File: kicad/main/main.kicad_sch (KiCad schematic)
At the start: 29 parts, among them J1 Barrel_Jack_MountingPin, SW1 Reset, SW2 SW_DIP_x08, U1 GAL16V8, U2 Z80CPU, U3 DS1813-5+, U4 AS6C4008-55PCN, U5 L7805, U6 74HC273, U7 27C512, U8 74HC244, X1 4 MHz

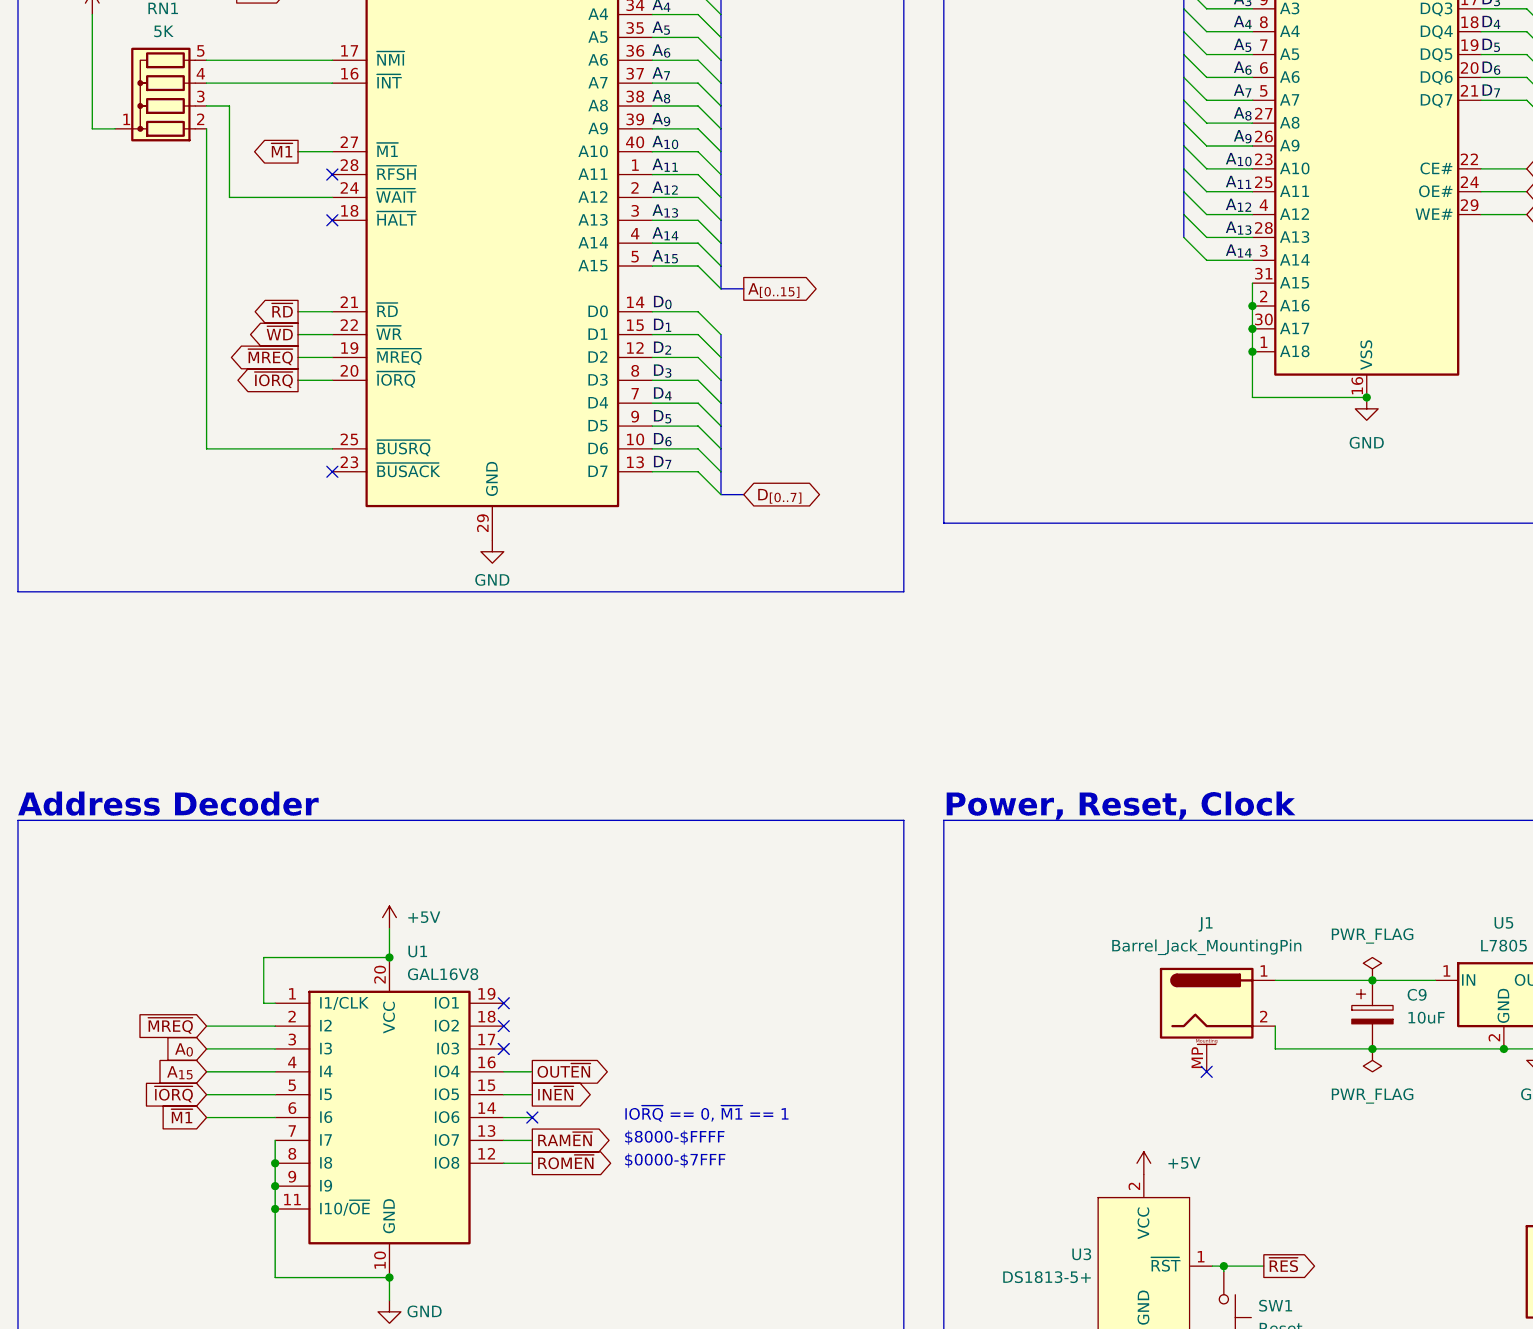
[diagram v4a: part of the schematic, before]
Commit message: Fix RAM CE2, add /RFSH
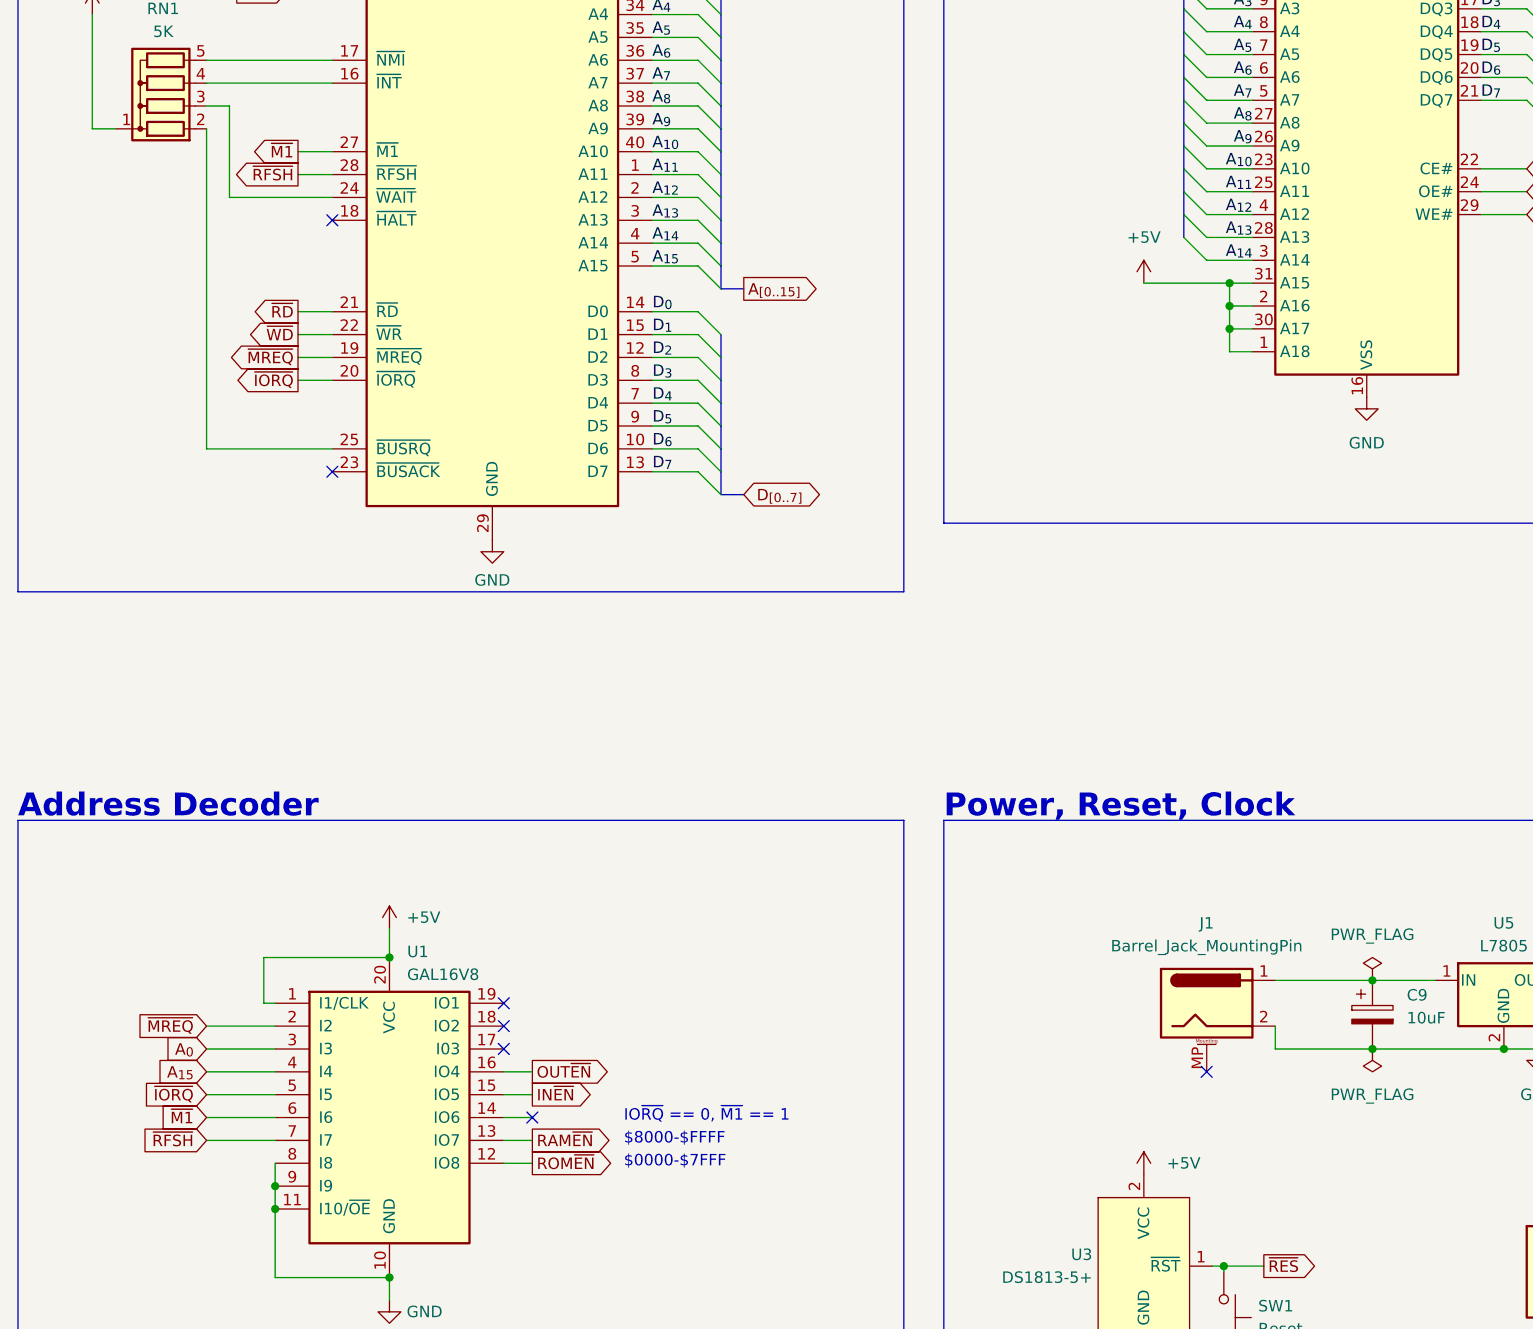
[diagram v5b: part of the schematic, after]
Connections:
- net +5V: now also U4.1 (A18), U4.2 (A16), U4.30 (A17), U4.31 (A15)
- net GND: no longer U1.7 (I7), U4.1 (A18), U4.2 (A16), U4.30 (A17), U4.31 (A15)
- net ~{RFSH}: now reaches U2.28 (~{RFSH})
- net ~{RFSH}: now also U1.7 (I7)
- no-connect marks 12 -> 11
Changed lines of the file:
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@@
   (junction (at 302.26 166.37) (diameter 0) (color 0 0 0 0)
   )
+  (junction (at 151.13 74.295) (diameter 0) (color 0 0 0 0)
+  )
   (junction (at 68.58 219.075) (diameter 0) (color 0 0 0 0)
   )
@@
   (junction (at 302.26 171.45) (diameter 0) (color 0 0 0 0)
   )
-  (junction (at 153.67 76.835) (diameter 0) (color 0 0 0 0)
-  )
   (junction (at 167.005 149.225) (diameter 0) (color 0 0 0 0)
   )
@@
   (junction (at 302.26 168.91) (diameter 0) (color 0 0 0 0)
   )
-  (junction (at 153.67 79.375) (diameter 0) (color 0 0 0 0)
-  )
   (junction (at 333.375 173.99) (diameter 0) (color 0 0 0 0)
   )
@@
   (junction (at 83.82 231.775) (diameter 0) (color 0 0 0 0)
   )
-  (junction (at 166.37 84.455) (diameter 0) (color 0 0 0 0)
-  )
   (junction (at 83.82 219.075) (diameter 0) (color 0 0 0 0)
   )
@@
   (junction (at 335.915 176.53) (diameter 0) (color 0 0 0 0)
   )
+  (junction (at 151.13 76.835) (diameter 0) (color 0 0 0 0)
+  )
   (junction (at 337.82 181.61) (diameter 0) (color 0 0 0 0)
   )
   (junction (at 60.96 219.075) (diameter 0) (color 0 0 0 0)
   )
+  (junction (at 151.13 71.755) (diameter 0) (color 0 0 0 0)
+  )
   (junction (at 53.34 231.775) (diameter 0) (color 0 0 0 0)
   )
   (junction (at 45.72 231.775) (diameter 0) (color 0 0 0 0)
   )
-  (junction (at 153.67 74.295) (diameter 0) (color 0 0 0 0)
-  )
   (junction (at 64.77 231.775) (diameter 0) (color 0 0 0 0)
   )
@@
   )
   (junction (at 45.085 172.085) (diameter 0) (color 0 0 0 0)
-  )
-  (junction (at 45.085 169.545) (diameter 0) (color 0 0 0 0)
   )
   (no_connect (at 73.66 164.465))
@@
   (no_connect (at 70.485 156.845))
   (no_connect (at 70.485 151.765))
-  (no_connect (at 51.435 59.69))
   (bus_entry (at 92.075 87.63) (size 2.54 2.54)
     (stroke (width 0) (type default))
@@
     (stroke (width 0) (type default))
   )
-  (wire (pts (xy 153.67 79.375) (xy 153.67 84.455))
-    (stroke (width 0) (type default))
-  )
   (wire (pts (xy 247.015 54.61) (xy 241.935 54.61))
     (stroke (width 0) (type default))
@@
     (stroke (width 0) (type default))
   )
-  (wire (pts (xy 45.085 167.005) (xy 45.085 169.545))
-    (stroke (width 0) (type default))
-  )
   (bus (pts (xy 186.69 36.195) (xy 186.69 38.735))
     (stroke (width 0) (type default))
@@
     (stroke (width 0) (type default))
   )
+  (wire (pts (xy 151.13 74.295) (xy 153.67 74.295))
+    (stroke (width 0) (type default))
+  )
   (wire (pts (xy 320.675 153.67) (xy 320.675 161.29))
     (stroke (width 0) (type default))
@@
     (stroke (width 0) (type default))
   )
+  (wire (pts (xy 151.13 79.375) (xy 153.67 79.375))
+    (stroke (width 0) (type default))
+  )
   (bus (pts (xy 239.395 52.07) (xy 239.395 49.53))
     (stroke (width 0) (type default))
@@
     (stroke (width 0) (type default))
   )
-  (wire (pts (xy 153.67 71.755) (xy 153.67 74.295))
-    (stroke (width 0) (type default))
-  )
   (bus (pts (xy 146.05 31.115) (xy 139.7 31.115))
     (stroke (width 0) (type default))
@@
     (stroke (width 0) (type default))
   )
+  (wire (pts (xy 151.13 76.835) (xy 151.13 74.295))
+    (stroke (width 0) (type default))
+  )
   (bus (pts (xy 239.395 62.23) (xy 239.395 59.69))
     (stroke (width 0) (type default))
@@
     (stroke (width 0) (type default))
   )
+  (wire (pts (xy 151.13 74.295) (xy 151.13 71.755))
+    (stroke (width 0) (type default))
+  )
   (wire (pts (xy 363.22 176.53) (xy 368.3 176.53))
     (stroke (width 0) (type default))
@@
     (stroke (width 0) (type default))
   )
+  (wire (pts (xy 141.605 71.755) (xy 151.13 71.755))
+    (stroke (width 0) (type default))
+  )
   (wire (pts (xy 267.335 36.83) (xy 272.415 36.83))
     (stroke (width 0) (type default))
@@
     (stroke (width 0) (type default))
   )
-  (wire (pts (xy 153.67 84.455) (xy 166.37 84.455))
+  (wire (pts (xy 151.13 76.835) (xy 153.67 76.835))
     (stroke (width 0) (type default))
   )
@@
     (stroke (width 0) (type default))
   )
+  (wire (pts (xy 151.13 71.755) (xy 153.67 71.755))
+    (stroke (width 0) (type default))
+  )
   (wire (pts (xy 86.995 44.45) (xy 92.075 44.45))
     (stroke (width 0) (type default))
@@
     (stroke (width 0) (type default))
   )
+  (wire (pts (xy 51.435 59.69) (xy 47.625 59.69))
+    (stroke (width 0) (type default))
+  )
   (wire (pts (xy 232.41 179.705) (xy 237.49 179.705))
     (stroke (width 0) (type default))
@@
     (stroke (width 0) (type default))
   )
+  (wire (pts (xy 37.465 167.005) (xy 45.085 167.005))
+    (stroke (width 0) (type default))
+  )
   (bus (pts (xy 146.05 59.055) (xy 146.05 56.515))
     (stroke (width 0) (type default))
@@
     (stroke (width 0) (type default))
   )
-  (wire (pts (xy 153.67 76.835) (xy 153.67 79.375))
-    (stroke (width 0) (type default))
-  )
   (wire (pts (xy 150.495 180.975) (xy 149.225 180.975))
     (stroke (width 0) (type default))
   )
-  (wire (pts (xy 153.67 74.295) (xy 153.67 76.835))
-    (stroke (width 0) (type default))
-  )
   (bus (pts (xy 274.955 41.91) (xy 274.955 44.45))
     (stroke (width 0) (type default))
@@
   )
   (wire (pts (xy 247.015 64.77) (xy 241.935 64.77))
+    (stroke (width 0) (type default))
+  )
+  (wire (pts (xy 151.13 79.375) (xy 151.13 76.835))
     (stroke (width 0) (type default))
   )
@@
     )
   )
+  (global_label "~{RFSH}" (shape input) (at 37.465 167.005 180) (fields_autoplaced)
+    (effects (font (size 1.27 1.27)) (justify right))
+    (property "Intersheetrefs" "${INTERSHEET_REFS}" (at 29.6606 167.005 0)
+      (effects (font (size 1.27 1.27)) (justify right) hide)
+    )
+  )
   (global_label "CLK" (shape output) (at 196.85 181.61 0) (fields_autoplaced)
     (effects (font (size 1.27 1.27)) (justify left))
@@
     (property "Intersheetrefs" "${INTERSHEET_REFS}" (at 193.3453 59.055 0)
       (effects (font (size 1.27 1.27)) (justify left) hide)
+    )
+  )
+  (global_label "~{RFSH}" (shape output) (at 47.625 59.69 180) (fields_autoplaced)
+    (effects (font (size 1.27 1.27)) (justify right))
+    (property "Intersheetrefs" "${INTERSHEET_REFS}" (at 39.8206 59.69 0)
+      (effects (font (size 1.27 1.27)) (justify right) hide)
     )
   )
@@
         )
       )
+    )
+  )
+  (symbol (lib_id "power:+5V") (at 141.605 71.755 0) (unit 1)
+    (in_bom yes) (on_board yes) (dnp no) (fields_autoplaced)
+    (property "Reference" "#PWR025" (at 141.605 75.565 0)
+      (effects (font (size 1.27 1.27)) hide)
+    )
+    (property "Value" "+5V" (at 141.605 66.675 0)
+      (effects (font (size 1.27 1.27)))
+    )
+    (property "Footprint" "" (at 141.605 71.755 0)
+      (effects (font (size 1.27 1.27)) hide)
+    )
+    (property "Datasheet" "" (at 141.605 71.755 0)
+      (effects (font (size 1.27 1.27)) hide)
+    )
+    (pin "1")
+    (instances
+      (project "main"
+        (path "/234daa3c-bbc3-4e0e-9846-fc4a6309b941"
+          (reference "#PWR025") (unit 1)
+        )
+      )

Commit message: Add new buffers
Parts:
- added U10, U11, U12: 74LS244, Package_DIP:DIP-20_W7.62mm_Socket, symbol 74xx:74LS244
- added U13: 74LS14, symbol 74xx:74LS14
- added U9: 74LS245, Package_DIP:DIP-20_W7.62mm_Socket, symbol 74xx:74LS245
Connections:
- net +5V: now also SW2.1, SW2.2, SW2.3, SW2.4, SW2.5, SW2.6, SW2.7, SW2.8, U10.20 (VCC), U11.20 (VCC), U12.20 (VCC), U13.14 (VCC), U9.20 (VCC); no longer RN3.1 (common)
- net A_{0}: now also U10.18 (O0a); no longer U2.30 (A0)
- net A_{10}: now also U11.14 (O2a); no longer U2.40 (A10)
- net A_{11}: now also U11.12 (O3a); no longer U2.1 (A11)
- net A_{12}: now also U11.9 (O0b); no longer U2.2 (A12)
- net A_{13}: now also U11.7 (O1b); no longer U2.3 (A13)
- net A_{14}: now also U11.5 (O2b); no longer U2.4 (A14)
- net A_{15}: now also U11.3 (O3b); no longer U2.5 (A15)
- net A_{1}: now also U10.16 (O1a); no longer U2.31 (A1)
- net A_{2}: now also U10.14 (O2a); no longer U2.32 (A2)
- net A_{3}: now also U10.12 (O3a); no longer U2.33 (A3)
- net A_{4}: now also U10.9 (O0b); no longer U2.34 (A4)
- net A_{5}: now also U10.7 (O1b); no longer U2.35 (A5)
- net A_{6}: now also U10.5 (O2b); no longer U2.36 (A6)
- net A_{7}: now also U10.3 (O3b); no longer U2.37 (A7)
- net A_{8}: now also U11.18 (O0a); no longer U2.38 (A8)
- net A_{9}: now also U11.16 (O1a); no longer U2.39 (A9)
- net D_{0}: now also U9.18 (B0); no longer U2.14 (D0)
- net D_{1}: now also U9.17 (B1); no longer U2.15 (D1)
- net D_{2}: now also U9.16 (B2); no longer U2.12 (D2)
- net D_{3}: now also U9.15 (B3); no longer U2.8 (D3)
- net D_{4}: now also U9.14 (B4); no longer U2.7 (D4)
- net D_{5}: now also U9.13 (B5); no longer U2.9 (D5)
- net D_{6}: now also U9.12 (B6); no longer U2.10 (D6)
- net D_{7}: now also U9.11 (B7); no longer U2.13 (D7)
- net GND: now also RN3.1 (common), U10.1 (OEa), U10.10 (GND), U10.19 (OEb), U11.1 (OEa), U11.10 (GND), U11.19 (OEb), U12.1 (OEa), U12.10 (GND), U12.19 (OEb), U13.7 (GND), U9.10 (GND), U9.19 (CE); no longer SW2.1, SW2.2, SW2.3, SW2.4, SW2.5, SW2.6, SW2.7, SW2.8
- net ~{RD}: now also U12.18 (O0a); no longer U2.21 (~{RD})
- net ~{WD}: now also U12.16 (O1a), U13.1; no longer U2.22 (~{WR})
- net at BAR1.1 (A): now also U6.19 (Q7); no longer U6.2 (Q0)
- net at BAR1.13 (K): now also RN2.2 (R1); no longer RN2.9 (R8)
- net at BAR1.14 (K): now also RN2.3 (R2); no longer RN2.8 (R7)
- net at BAR1.15 (K): now also RN2.4 (R3); no longer RN2.7 (R6)
- net at BAR1.16 (K): now also RN2.5 (R4); no longer RN2.6 (R5)
- net at BAR1.17 (K): now also RN2.6 (R5); no longer RN2.5 (R4)
- net at BAR1.18 (K): now also RN2.7 (R6); no longer RN2.4 (R3)
- net at BAR1.19 (K): now also RN2.8 (R7); no longer RN2.3 (R2)
- net at BAR1.2 (A): now also U6.16 (Q6); no longer U6.5 (Q1)
- net at BAR1.20 (K): now also RN2.9 (R8); no longer RN2.2 (R1)
- net at BAR1.3 (A): now also U6.15 (Q5); no longer U6.6 (Q2)
- net at BAR1.4 (A): now also U6.12 (Q4); no longer U6.9 (Q3)
- net at BAR1.5 (A): now also U6.9 (Q3); no longer U6.12 (Q4)
- net at BAR1.6 (A): now also U6.6 (Q2); no longer U6.15 (Q5)
- net at BAR1.7 (A): now also U6.5 (Q1); no longer U6.16 (Q6)
- net at BAR1.8 (A): now also U6.2 (Q0); no longer U6.19 (Q7)
- net at RN3.8 (R7), U8.13 (2A2): now also SW2.15; no longer SW2.10
- net at RN3.7 (R6), U8.15 (2A1): now also SW2.14; no longer SW2.11
- net at RN3.6 (R5), U8.17 (2A0): now also SW2.13; no longer SW2.12
- net at RN3.5 (R4), U8.8 (1A3): now also SW2.12; no longer SW2.13
- net at RN3.4 (R3), U8.6 (1A2): now also SW2.11; no longer SW2.14
- net at RN3.3 (R2), U8.4 (1A1): now also SW2.10; no longer SW2.15
- net at RN3.2 (R1), U8.2 (1A0): now also SW2.9; no longer SW2.16
- net at RN3.9 (R8), U8.11 (2A3): now also SW2.16; no longer SW2.9
- new net: U13.2, U9.1 (A->B)
- new net A^{u}_{0}: U10.2 (I0a), U2.30 (A0)
- new net A^{u}_{10}: U11.6 (I2a), U2.40 (A10)
- new net A^{u}_{11}: U11.8 (I3a), U2.1 (A11)
- new net A^{u}_{12}: U11.11 (I0b), U2.2 (A12)
- new net A^{u}_{13}: U11.13 (I1b), U2.3 (A13)
- new net A^{u}_{14}: U11.15 (I2b), U2.4 (A14)
- new net A^{u}_{15}: U11.17 (I3b), U2.5 (A15)
- new net A^{u}_{1}: U10.4 (I1a), U2.31 (A1)
- new net A^{u}_{2}: U10.6 (I2a), U2.32 (A2)
- new net A^{u}_{3}: U10.8 (I3a), U2.33 (A3)
- new net A^{u}_{4}: U10.11 (I0b), U2.34 (A4)
- new net A^{u}_{5}: U10.13 (I1b), U2.35 (A5)
- new net A^{u}_{6}: U10.15 (I2b), U2.36 (A6)
- new net A^{u}_{7}: U10.17 (I3b), U2.37 (A7)
- new net A^{u}_{8}: U11.2 (I0a), U2.38 (A8)
- new net A^{u}_{9}: U11.4 (I1a), U2.39 (A9)
- new net D^{u}_{0}: U2.14 (D0), U9.2 (A0)
- new net D^{u}_{1}: U2.15 (D1), U9.3 (A1)
- new net D^{u}_{2}: U2.12 (D2), U9.4 (A2)
- new net D^{u}_{3}: U2.8 (D3), U9.5 (A3)
- new net D^{u}_{4}: U2.7 (D4), U9.6 (A4)
- new net D^{u}_{5}: U2.9 (D5), U9.7 (A5)
- new net D^{u}_{6}: U2.10 (D6), U9.8 (A6)
- new net D^{u}_{7}: U2.13 (D7), U9.9 (A7)
- new net ~{RD^{u}}: U12.2 (I0a), U2.21 (~{RD})
- new net ~{WD^{u}}: U12.4 (I1a), U2.22 (~{WR})
- no-connect marks 11 -> 33
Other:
- note added: "CPU & Buffers"
- note added: "This inverter also adds an important delay which is needed by slow chips that require non-zero data hold time. When /WR de-asserts, it not only tells devices to latch, but also turns off the data transceiver. With this delay, our data bus transceiver will switch direction with a slight delay, giving the device some time to latch the data."
- note removed: "CPU"
- moved on the sheet: BAR1, C1, C2, C3, C4, C5, C6, C7, C8, C9, H1, H2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
